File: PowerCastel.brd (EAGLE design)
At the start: 27.9 x 17.1 mm, 22 parts, among them U1 TPS61090RSAR, U2 MCP73871

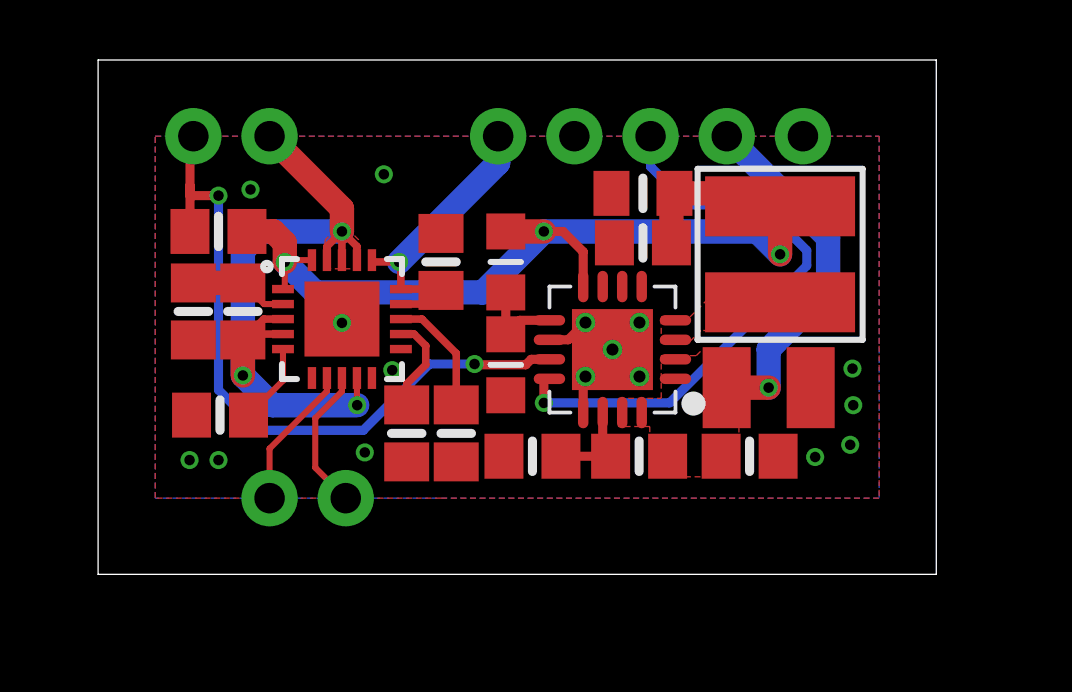
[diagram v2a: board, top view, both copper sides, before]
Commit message: Updated design
New design has improved ground plane and has better support for external LEDs.
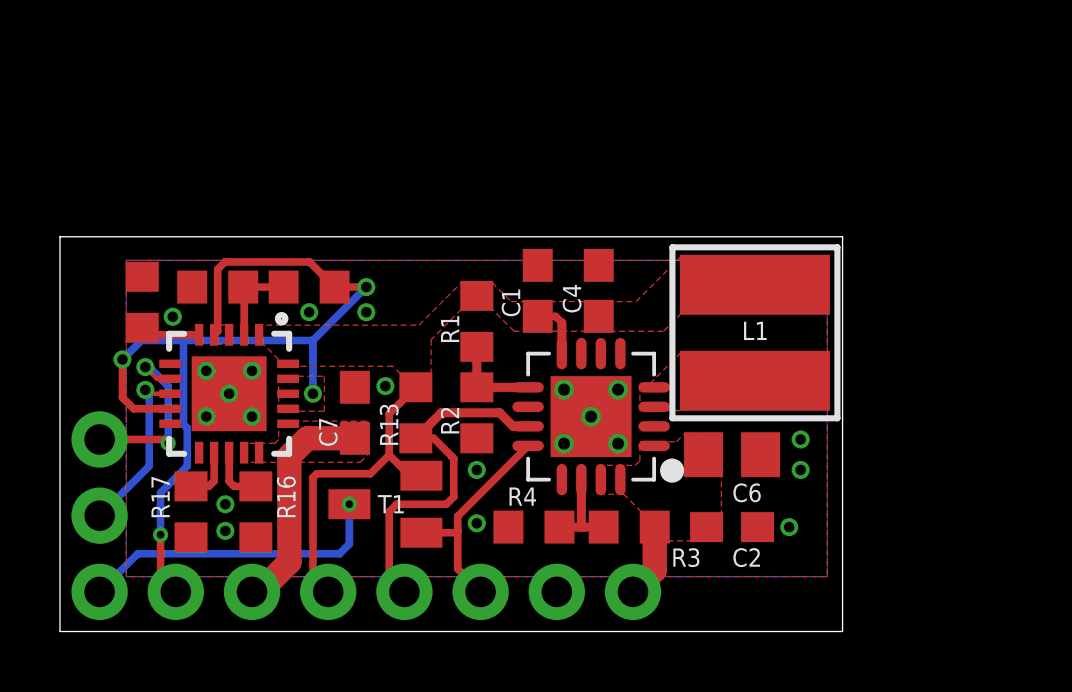
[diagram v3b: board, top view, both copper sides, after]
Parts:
- added T1: MMUN2133LT1G, transistor:SC59-BEC
- C1, C2, C7: device microbuilder:0805-NO -> rcl:C0603
- C4: device microbuilder:0805_10MGAP -> rcl:C0603
- C6: device rcl:C1210 -> rcl:C0805
- J1: device SparkFun-Connectors:1X02_NO_SILK -> SparkFun-Connectors:1X07_NO_SILK
- J2: device SparkFun-Connectors:1X03_NO_SILK -> SparkFun-Connectors:1X01_NO_SILK
- J3, J4: device SparkFun-Connectors:1X02_NO_SILK -> SparkFun-Connectors:1X01_NO_SILK
- R1, R2: device microbuilder:_0805MP -> rcl:R0603
- R13, R16, R17, R3, R4, R6, R7, THERM: device microbuilder:0805-NO -> rcl:R0603
- moved J2 25.5 mm to (1.32, 6.40), turned to 0 degrees
- moved J3 18.3 mm to (1.32, 3.86)
- moved J1 15.2 mm to (3.86, 1.32)
- moved R13 8.93 mm to (11.9, 7.29), turned to 270 degrees
- moved J4 8.78 mm to (1.32, 1.32), turned to 0 degrees
- moved R17 7.65 mm to (4.37, 3.99)
- moved R16 7.17 mm to (6.53, 3.99)
- moved C7 5.79 mm to (9.83, 7.29)
- moved THERM 4.57 mm to (2.74, 11.0), turned to 270 degrees
- moved U2 4.51 mm to (5.64, 7.92), turned to 270 degrees
- moved C1 3.85 mm to (15.9, 11.4), turned to 90 degrees
- moved C4 3.57 mm to (18.0, 11.4), turned to 90 degrees
- moved L1 2.75 mm to (23.2, 9.96)
- moved C6 2.55 mm to (22.4, 5.89)
- moved C2 2.43 mm to (22.4, 3.48)
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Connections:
- removed net CHARGING: J4.1, U2.P$8
- new net CHRG: J3.1, U2.P$8
- new net LOW: J4.1, T1.C
- net 5.0V: now also J1.7; no longer J2.2
- net DONE: now also J2.1; no longer J4.2
- net ENABLE: now also J1.4; no longer J1.1
- net GND: now also J1.6; no longer J2.1, J3.2
- net LBO: now also J1.5, T1.B; no longer J2.3
- net VBAT: now also J1.3, T1.E
- net VBUS: now also J1.1; no longer J1.2
- net VLIPO: now also J1.2; no longer J3.1
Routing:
- net VBAT: track 33.0 -> 12.8 mm, vias 3 -> 0
- net LBO: track 19.5 -> 7.39 mm, vias 1 -> 0
- net ENABLE: track 23.6 -> 12.3 mm, vias 2 -> 0
- net LOW: track 0.00 -> 10.3 mm, vias 0 -> 1
- net 5.0V: track 12.0 -> 2.46 mm, vias 1 -> 0
- net VBUS: track 24.3 -> 30.6 mm, vias 3 -> 4
- net CHRG: track 0.00 -> 5.81 mm, vias 0 -> 1
- net CHARGING: track 4.79 -> 0.00 mm
- net GND: track 4.07 -> 0.00 mm, vias 11 -> 16
- net VLIPO: track 10.3 -> 7.62 mm, vias 1 -> 0
- net N$16: track 4.04 -> 1.91 mm
- net DONE: track 4.80 -> 6.26 mm, vias 0 -> 2
- net N$13: track 3.22 -> 1.79 mm
- net N$10: track 2.68 -> 1.99 mm
- added copper zone on layer 1, net VBAT
- added copper zone on layer 1, net VLIPO
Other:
- board size 27.9 x 17.1 mm -> 26.1 x 13.2 mm
- board text added: "CHRG"
- board text added: "LIPO"
- board text added: "LOW"
- board text added: "VBAT"
- board text added: "VBUS"
- board text removed: "BAT"
- board text removed: "CHG"
- board text removed: "USB"
